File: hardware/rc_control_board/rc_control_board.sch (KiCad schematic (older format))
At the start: 53 parts, among them J1 PWR, J10 3V3_Con, J2 SWD Con, J3 I2C1, J4 GPS, J5 SPI1, J6 UART_DEBUG, J7 UART_NAV_BOARD, J8 MOTOR_CTRL, J9 SERVO_CTRL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

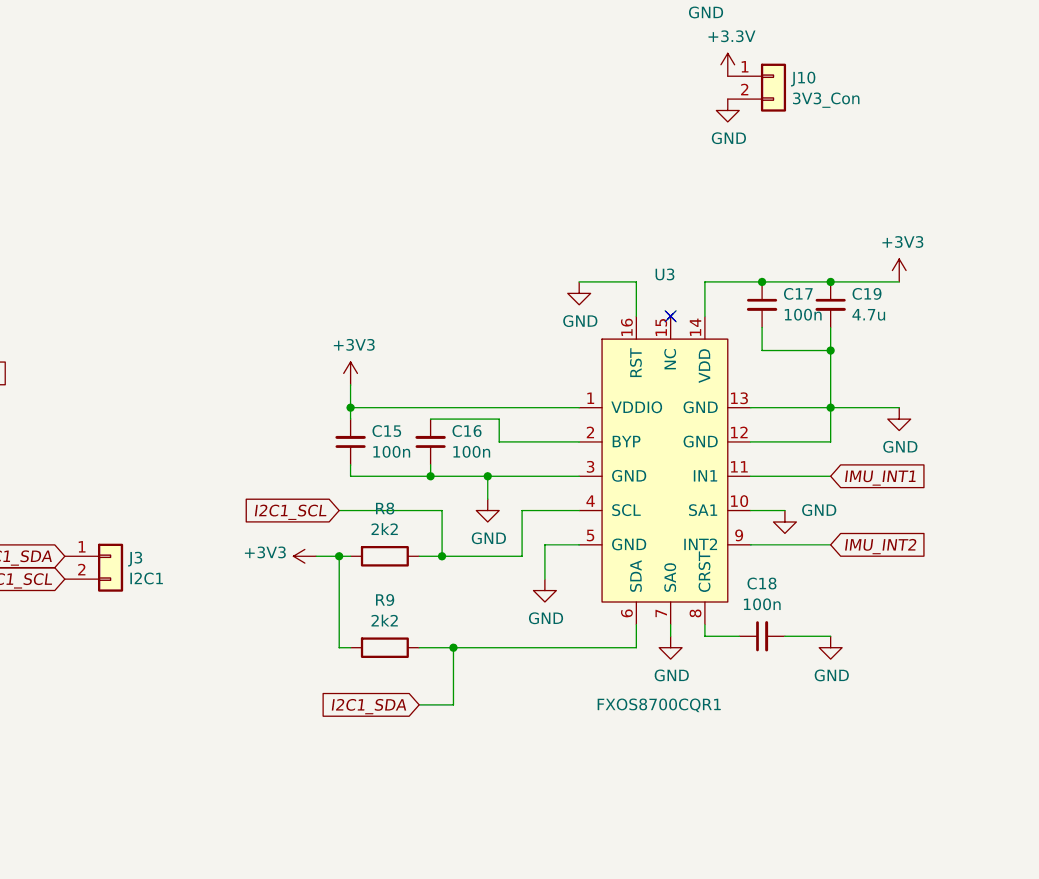
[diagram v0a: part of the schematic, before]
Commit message: HW: Fix layout errors for IMU
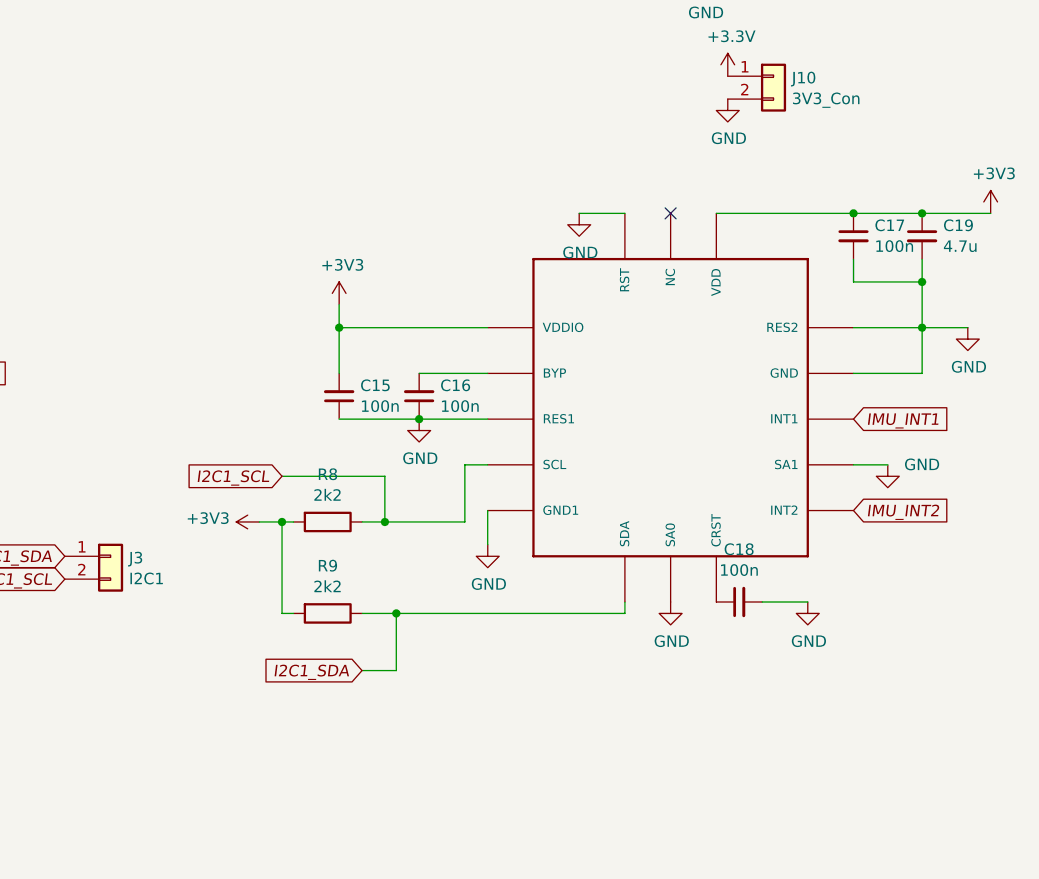
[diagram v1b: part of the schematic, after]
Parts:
- removed U3: FXOS8700CQR1, Package_DFN_QFN:QFN-16-1EP_3x3mm_P0.5mm_EP1.75x1.75mm, symbol rc_car_control:FXOS8700CQR1
- added U4: FXOS8700CQ, rc_control_board:FSOS8700CQ_PKG, symbol FXOS8700CQ:FXOS8700CQ
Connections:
- net +3V3: now also U4.P$1 (VDDIO), U4.P$14 (VDD)
- net GND: now also U4.P$10 (SA1), U4.P$12 (GND), U4.P$13 (RES2), U4.P$16 (RST), U4.P$3 (RES1), U4.P$5 (GND1), U4.P$7 (SA0)
- net I2C1_SCL: now also U4.P$4 (SCL)
- net I2C1_SDA: now also U4.P$6 (SDA)
- net IMU_INT1: now also U4.P$11 (INT1)
- net IMU_INT2: now also U4.P$9 (INT2)
- net at C16.2: now also U4.P$2 (BYP)
- net at C18.1: now also U4.P$8 (CRST)
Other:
- moved on the sheet: C15, C16, C17, C18, C19, R8, R9
